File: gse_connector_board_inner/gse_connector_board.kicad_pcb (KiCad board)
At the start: 2 copper layers, 52.2 x 27 mm, 29 parts, among them J1 arming_connector, J2 gse_com_connector, J3 chg_connector, J4 Conn_02x03_Top_Bottom, J5 Conn_02x02_Top_Bottom, U7 ISO1044BD, U9 MCP2562-E-SN

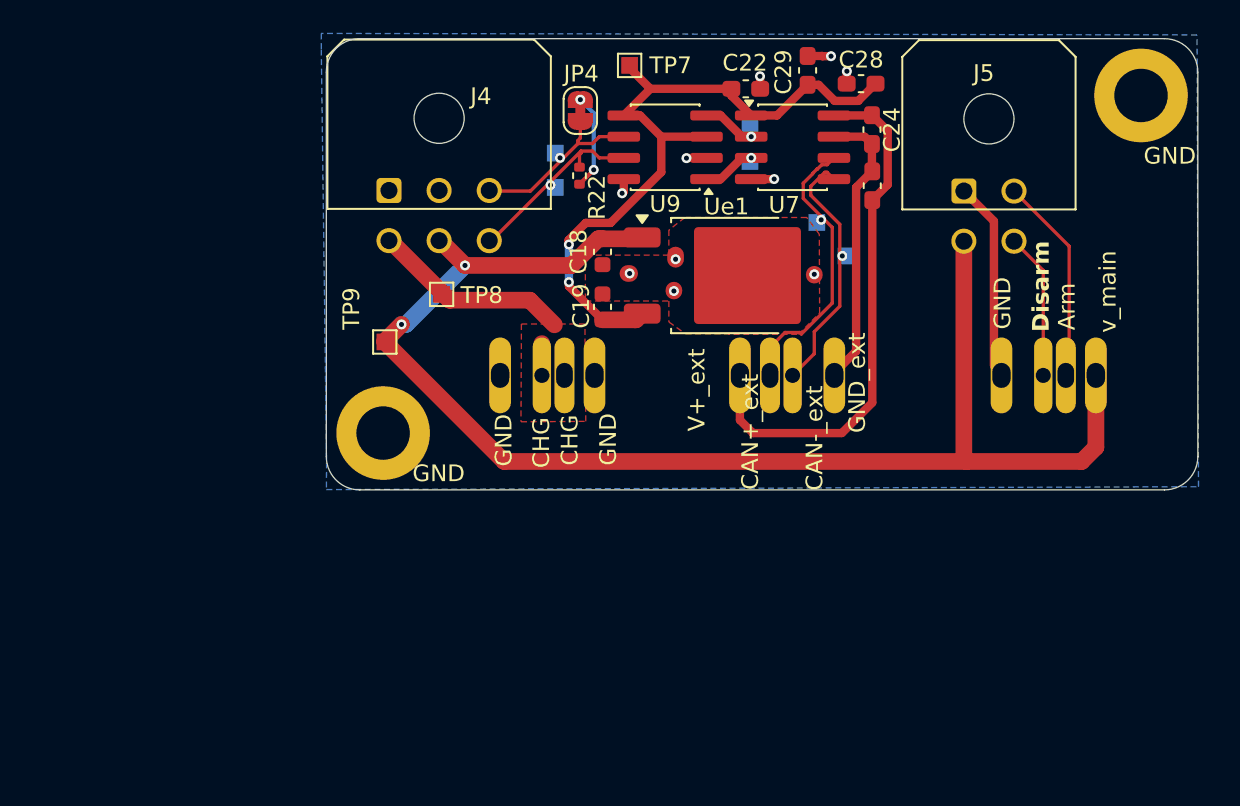
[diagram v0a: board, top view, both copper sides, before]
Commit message: adapted footprints, scematics and routing
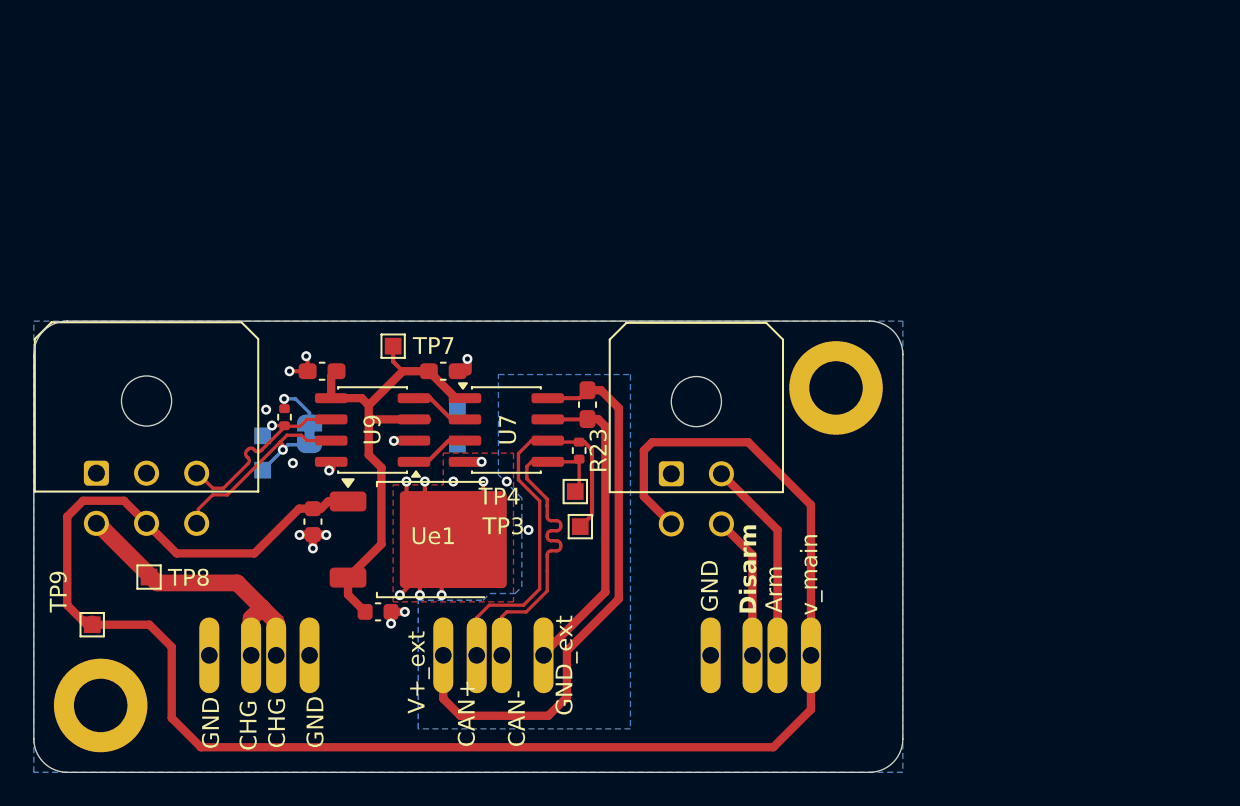
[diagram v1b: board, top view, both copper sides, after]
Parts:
- removed C24: 470n, Capacitor_SMD:C_0603_1608Metric_Pad1.08x0.95mm_HandSolder
- removed C28: 100n, Capacitor_SMD:C_0603_1608Metric_Pad1.08x0.95mm_HandSolder
- added R23: 120, Resistor_SMD:R_0402_1005Metric, F.Cu at (132.6, 80.8)
- JP4: moved to B.Cu
- TP3, TP4: moved to F.Cu
- moved C29 34.2 mm to (117.2, 76.0), turned to 0 degrees
- moved H1 25.3 mm to (148.0, 77.0)
- moved JP4 25.2 mm to (116.5, 79.8), turned to -90 degrees
- moved C22 24.8 mm to (124.5, 76.0)
- moved U9 24.3 mm to (120.3, 79.5)
- moved TP8 24.3 mm to (106.9, 88.3)
- moved G*** 24.3 mm to (115.7, 75.3)
- moved TP5 24.3 mm to (125.3, 78.3)
- moved J4 24.3 mm to (103.7, 82.1)
- moved J5 24.3 mm to (138.1, 82.1)
- moved TP6 24.3 mm to (125.3, 80.4)
- moved TP9 24.3 mm to (103.5, 91.2)
- moved TP1 24.3 mm to (113.7, 81.9)
- moved TP2 24.3 mm to (113.7, 79.9)
- moved J2 24.2 mm to (128.0, 90.0)
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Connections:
- JP4 pad 1: CAN_1- -> Net-(JP4-A)
- JP4 pad 2: Net-(JP4-B) -> CAN_1+
- R22 pad 1: CAN_1+ -> Net-(JP4-A)
- R22 pad 2: Net-(JP4-B) -> CAN_1-
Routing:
- net main_voltage: track 83.5 -> 105.7 mm, vias 2 -> 0
- net GND: track 18.9 -> 35.4 mm, vias 10 -> 21
- net +5V: track 43.1 -> 30.6 mm, vias 2 -> 0
- net CAN_ext+: track 19.4 -> 27.4 mm, vias 1 -> 0
- net CHG: track 13.8 -> 20.1 mm
- net CAN_ext-: track 16.7 -> 22.8 mm, vias 1 -> 0
- net Net-(JP4-B): track 5.74 -> 0.00 mm, vias 2 -> 0
- net CAN_1+: track 11.7 -> 15.1 mm
- net Net-(JP4-A): track 0.00 -> 3.07 mm, vias 0 -> 1
- net +V_EXT: track 31.9 -> 34.4 mm
- net GND_EXT: track 17.3 -> 18.9 mm, vias 0 -> 1
- net CAN_1-: track 11.1 -> 12.4 mm
- net Net-(U7-TXD): track 3.73 -> 4.95 mm, vias 1 -> 0
- net Net-(U7-RXD): track 3.45 -> 3.83 mm, vias 1 -> 0
- added copper zone on B.Cu, net GND_EXT
- removed copper zone on F.Cu, net CHG
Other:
- board size 52.2 x 27 mm -> 52 x 27 mm
- board text removed: "CAN+_ext"
- board text removed: "CAN-_ext"
- board text removed: "J5"

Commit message: implemented changes
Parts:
- TP1, TP2, TP3, TP4, TP5, TP6, TP7, TP8, TP9: footprint TestPoint:TestPoint_Pad_1.0x1.0mm -> TestPoint:TestPoint_Pad_D1.5mm
- moved TP8 2.14 mm to (106.1, 90.3)
- moved TP6 1.57 mm to (123.8, 80.1)
- moved TP5 0.92 mm to (126.1, 77.8)
- moved G*** 0.43 mm to (115.7, 75.7)
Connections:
- J1 pad 1: main_voltage -> voltage_Arm
- J1 pad 4: GND -> GND_Arm
- J5 pad 1: GND -> GND_Arm
- J5 pad 3: main_voltage -> voltage_Arm
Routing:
- net main_voltage: track 105.7 -> 27.1 mm
- net voltage_Arm: track 0.00 -> 22.1 mm
- net GND_Arm: track 0.00 -> 11.8 mm
- net GND: track 35.4 -> 27.7 mm, vias 21 -> 18
- net Net-(U7-TXD): track 4.95 -> 7.79 mm, vias 0 -> 1
- net CHG: track 20.1 -> 22.4 mm
- net CAN_ext+: track 27.4 -> 25.1 mm
- net CAN_ext-: track 22.8 -> 20.7 mm
- net +5V: track 30.6 -> 29.3 mm
- net Net-(JP4-A): track 3.07 -> 2.38 mm
- net Net-(U7-RXD): track 3.83 -> 4.07 mm, vias 0 -> 1
- net GND_EXT: track 18.9 -> 18.8 mm, vias 1 -> 0
- added copper zone on B.Cu, net GND_Arm
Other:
- board text added: "+"
- board text added: "-"
- board text added: "CAN"
- board text added: "main"
- board text added: "v"
- board text added: "v_arm"

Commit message: cleanup silkscreen
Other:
- board text added: "120Ω"
- board text added: "Vcharg"
- board text added: "Vmain"
- board text added: "rev2"
- board text removed: "main"
- board text removed: "rev1"
- board text removed: "v"
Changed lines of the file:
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@@
 		(at 143.000001 95.999999 180)
 		(property "Reference" "J1"
-			(at 0 0.5 0)
+			(at -0.249999 -0.825001 0)
 			(unlocked yes)
 			(layer "B.SilkS")
@@
 			(at 2.2 -0.05 0)
 			(layer "B.SilkS")
+			(hide yes)
 			(effects
 				(font
@@
 	)
 	(gr_text "CHG"
-		(at 113.444044 98.717346 90)
-		(layer "F.SilkS")
-		(effects
-			(font
-				(size 1 1)
-				(thickness 0.15)
-			)
-			(justify left bottom)
-		)
-	)
-	(gr_text "CHG"
-		(at 115.144044 98.567346 90)
+		(at 114.425 98.55 90)
 		(layer "F.SilkS")
 		(effects
@@
 	)
 	(gr_text "Arm"
-		(at 144.894044 90.467346 90)
+		(at 145.25 90.575 90)
 		(layer "F.SilkS")
 		(effects
@@
 	)
 	(gr_text "v_main\n"
-		(at 147 90.617346 90)
+		(at 147.025 90.55 90)
 		(layer "F.SilkS")
 		(effects
@@
 	)
 	(gr_text "Disarm"
-		(at 143.344044 90.567346 90)
+		(at 143.65 90.5 90)
 		(layer "F.SilkS")
 		(effects
@@
 		)
 	)
+	(gr_text "Arming"
+		(at 145.544044 90.067346 -0)
+		(layer "B.SilkS")
+		(effects
+			(font
+				(size 1 1)
+				(thickness 0.1)
+			)
+			(justify left bottom mirror)
+		)
+	)
+	(gr_text "GND"
+		(at 106.9 80.85 0)
+		(layer "B.SilkS")
+		(effects
+			(font
+				(size 1 1)
+				(thickness 0.15)
+			)
+			(justify left bottom mirror)
+		)
+	)
+	(gr_text "CAN"
+		(at 111.4 81 0)
+		(layer "B.SilkS")
+		(effects
+			(font
+				(size 1 1)
+				(thickness 0.15)
+			)
+			(justify left bottom mirror)
+		)
+	)
+	(gr_text "-"
+		(at 112.2 82.525 0)
+		(layer "B.SilkS")
+		(effects
+			(font
+				(size 1 1)
+				(thickness 0.15)
+			)
+			(justify left bottom mirror)
+		)
+	)
+	(gr_text "+"
+		(at 112.2 85.55 0)
+		(layer "B.SilkS")
+		(effects
+			(font
+				(size 1 1)
+				(thickness 0.15)
+			)
+			(justify left bottom mirror)
+		)
+	)
 	(gr_text "GND"
 		(at 136.694044 82.717346 0)
@@
 			(font
 				(size 1 1)
-				(thickness 0.1)
+				(thickness 0.15)
 			)
 			(justify left bottom mirror)
@@
 			(font
 				(size 1 1)
-				(thickness 0.1)
-			)
-			(justify left bottom mirror)
-		)
-	)
-	(gr_text "Arming"
-		(at 145.544044 90.067346 -0)
-		(layer "B.SilkS")
-		(effects
-			(font
-				(size 1 1)
-				(thickness 0.1)
-			)
-			(justify left bottom mirror)
-		)
-	)
-	(gr_text "GND"
-		(at 106.9 80.85 0)
-		(layer "B.SilkS")
-		(effects
-			(font
-				(size 1 1)
-				(thickness 0.15)
-			)
-			(justify left bottom mirror)
-		)
-	)
-	(gr_text "CAN"
-		(at 111.4 81 0)
-		(layer "B.SilkS")
-		(effects
-			(font
-				(size 1 1)
-				(thickness 0.15)
-			)
-			(justify left bottom mirror)
-		)
-	)
-	(gr_text "+"
-		(at 112.1 82.6 0)
-		(layer "B.SilkS")
-		(effects
-			(font
-				(size 1 1)
-				(thickness 0.15)
-			)
-			(justify left bottom mirror)
-		)
-	)
-	(gr_text "-"
-		(at 112.2 85.7 0)
-		(layer "B.SilkS")
-		(effects
-			(font
-				(size 1 1)
 				(thickness 0.15)
 			)
@@
 		)
 	)
-	(gr_text "CHG"
-		(at 103.65 86.4 90)
+	(gr_text "Vcharg"
+		(at 104.25 86.125 90)
 		(layer "B.SilkS")
 		(effects
@@
 		)
 	)
-	(gr_text "main\n"
-		(at 106.35 86.1 90)
+	(gr_text "Vmain\n"
+		(at 106.55 85.925 90)
 		(layer "B.SilkS")
 		(effects
@@
 		)
 	)
-	(gr_text "rev1"
+	(gr_text "120Ω"
+		(at 117.775 81.975 270)
+		(layer "B.SilkS")
+		(effects
+			(font
+				(size 1 1)
+				(thickness 0.15)
+			)
+			(justify left bottom mirror)
+		)
+	)
+	(gr_text "rev2"
 		(at 130.094044 74.667346 0)
 		(layer "B.SilkS")
@@
 		)
 	)
-	(gr_text "v"
-		(at 101.9 84.95 0)
-		(layer "B.SilkS")
-		(effects
-			(font
-				(size 1.27 1.27)
-			)
-		)
-	)

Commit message: replace can isolation with mosfet
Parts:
- removed C18: 330n, Capacitor_SMD:C_0603_1608Metric
- removed C19: 100n, Capacitor_SMD:C_0603_1608Metric
- removed C22, C23, C29: 100n, Capacitor_SMD:C_0603_1608Metric_Pad1.08x0.95mm_HandSolder
- removed JP4: Jumper_2_Small_Open, Jumper:SolderJumper-2_P1.3mm_Bridged_RoundedPad1.0x1.5mm
- removed R22, R23: 120, Resistor_SMD:R_0402_1005Metric
- removed TP1, TP2, TP3, TP4, TP5, TP6, TP7, TP8, TP9: TestPoint, TestPoint:TestPoint_Pad_D1.5mm
- removed U7: ISO1044BD, Package_SO:SOIC-8_3.9x4.9mm_P1.27mm
- removed U9: MCP2562-E-SN, Package_SO:SOIC-8_3.9x4.9mm_P1.27mm
- removed Ue1: L7805, Package_TO_SOT_SMD:TO-252-2
- added J10: JST-GH 4Pin, Connector_JST:JST_GH_BM04B-GHS-TBT_1x04-1MP_P1.25mm_Vertical, F.Cu at (125.5, 76.6)
- added Q1: AO3400A, Package_TO_SOT_SMD:SOT-23, F.Cu at (125.2, 83.0)
- added R24: 120, Resistor_SMD:R_0402_1005Metric, F.Cu at (126.9, 84.6)
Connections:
- J2 pad 2: CAN_ext+ -> CAN_1+
- J2 pad 3: CAN_ext- -> CAN_1-
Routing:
- net +V_EXT: track 34.4 -> 0.00 mm
- net +5V: track 29.3 -> 0.00 mm
- net CAN_1-: track 12.5 -> 40.5 mm, vias 1 -> 0
- net main_voltage: track 27.1 -> 0.00 mm
- net GND: track 27.7 -> 2.02 mm, vias 18 -> 2
- net CAN_ext+: track 25.1 -> 0.00 mm
- net CAN_ext-: track 20.7 -> 0.00 mm
- net GND_EXT: track 18.8 -> 0.00 mm
- net CAN_1+: track 14.8 -> 30.8 mm, vias 1 -> 0
- net Net-(U7-TXD): track 7.79 -> 0.00 mm, vias 1 -> 0
- net Net-(U7-RXD): track 4.07 -> 0.00 mm, vias 1 -> 0
- net Net-(J10-Pin_4): track 0.00 -> 4.03 mm
- net Net-(Q1-S): track 0.00 -> 3.73 mm
- net Net-(JP4-A): track 2.38 -> 0.00 mm, vias 1 -> 0
- net CHG: track 22.4 -> 20.3 mm
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- removed copper zone on F.Cu, net GND

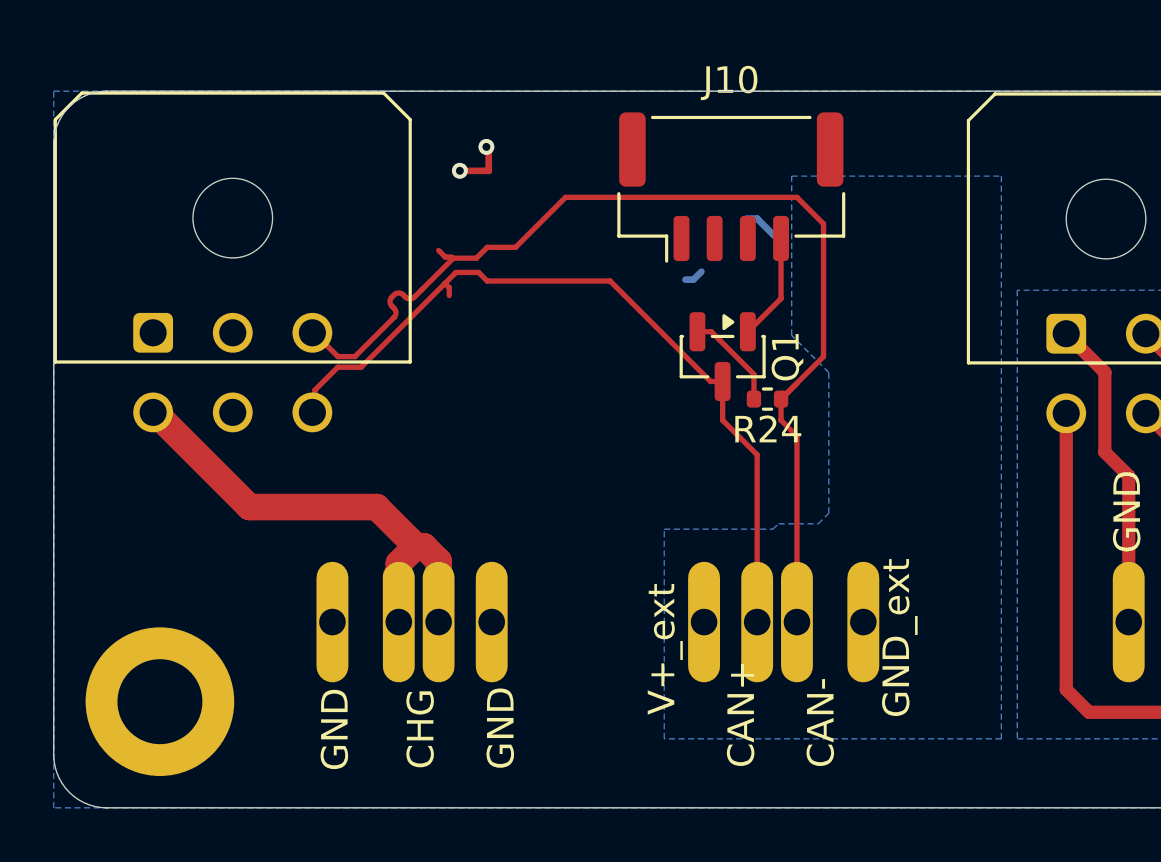
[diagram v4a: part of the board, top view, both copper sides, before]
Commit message: route new can isolation
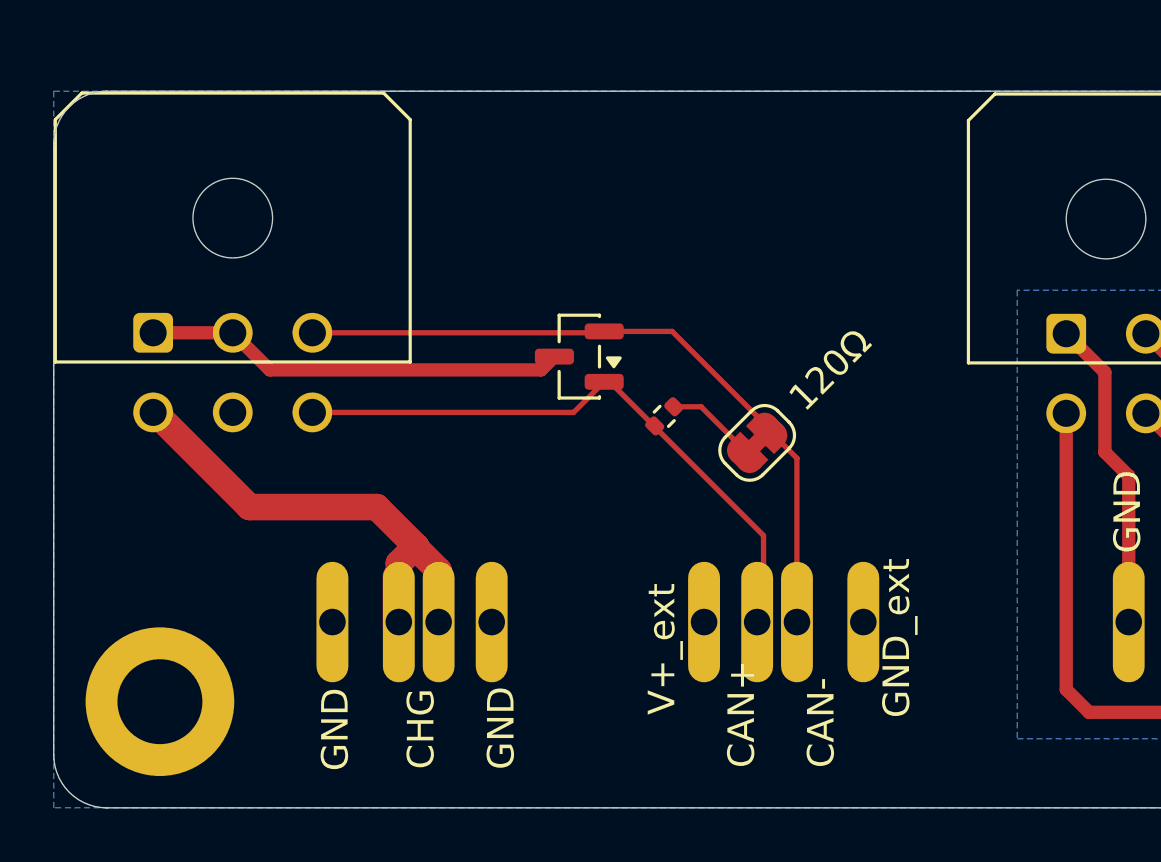
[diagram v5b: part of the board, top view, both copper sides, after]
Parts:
- removed J10: JST-GH 4Pin, Connector_JST:JST_GH_BM04B-GHS-TBT_1x04-1MP_P1.25mm_Vertical
- removed Q1: AO3400A, Package_TO_SOT_SMD:SOT-23
- added 120Ω: SolderJumper_2_Bridged, Jumper:SolderJumper-2_P1.3mm_Bridged_RoundedPad1.0x1.5mm, F.Cu at (126.5, 86.2)
- added D1: PESD2CAN, Package_TO_SOT_SMD:SOT-23, F.Cu at (119.8, 83.0)
- moved R24 3.94 mm to (123.0, 85.2), turned to -135 degrees
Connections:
- J2 pad 4: GND_EXT -> GND
- J4 pad 5: main_voltage -> unconnected-(J4-Pin_5-Pad5)
- R24 pad 1: CAN_1- -> Net-(JP1-A)
- R24 pad 2: Net-(Q1-S) -> CAN_1+
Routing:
- net CAN_1-: track 40.5 -> 26.5 mm
- net GND: track 2.02 -> 15.9 mm, vias 2 -> 0
- net CAN_1+: track 30.8 -> 24.2 mm
- net Net-(J10-Pin_4): track 4.03 -> 0.00 mm
- net Net-(JP1-A): track 0.00 -> 3.73 mm
- net Net-(Q1-S): track 3.73 -> 0.00 mm
- net (no net): track 2.04 -> 0.00 mm
- removed copper zone on B.Cu, net GND_EXT
